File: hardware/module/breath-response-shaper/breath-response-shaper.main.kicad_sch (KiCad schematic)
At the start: 13 parts

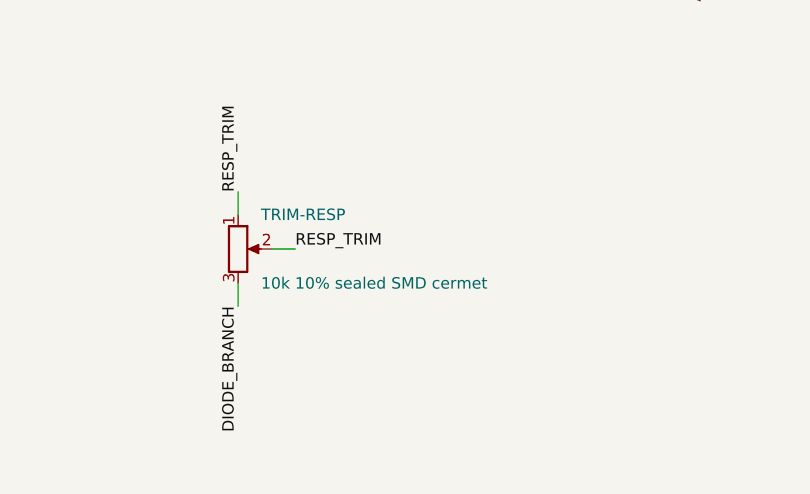
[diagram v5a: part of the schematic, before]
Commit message: #32: checkpoint - the owner's three answers and side-adjust trimmers
Owner decisions of 2026-10-04, recorded in ADR 0003/0004/0023/0024:
- WIDE's CMRR requirement band is DC to 7 kHz ("Keep 10 kHz, accept");
  cmrr-wide holds 58.5 dB there and records 10 kHz.
- D-TVS-BREATH is the PESD12VL1BA (19 pF), datasheet banked; PWR_GND
  held under -60 dB in each mode's band, WIDE at the accepted figure.
- The -12 V offset leg is filtered: R-BREATH-OFFNEG-A/-B 47.5k with
  C-BREATH-OFFNEG 1 uF at the split (6.7 Hz). Rest level +16 mV.
- The four trimmers are Bourns 3296X side-adjust, set with the module
  out of the rack; no rear-access windows. Current 3296 datasheet banked.

Sims are mid-run; their results land in the next commit.

Gate-Red: sim results stale or pre-change for receive-stage, power-entry, pitch-stage, mod-channels, shaper, system, breath-excitation-reference, digital-and-supervision and panel-led while they re-run on these inputs (checkpoint, as asked every 45 min); module-main and main-board .kicad_pcb parity with the new/changed parts (layout's, not touched here); main-board fab stale against the breath-adc sheet; module-main's existing routing/silk/acid-trap failures.

Co-Authored-By: Claude Opus 5.5 <noreply@anthropic.com>
Claude-Session: https://claude.ai/code/session_01LmB4muFXnoLprWX4JzuJ5A
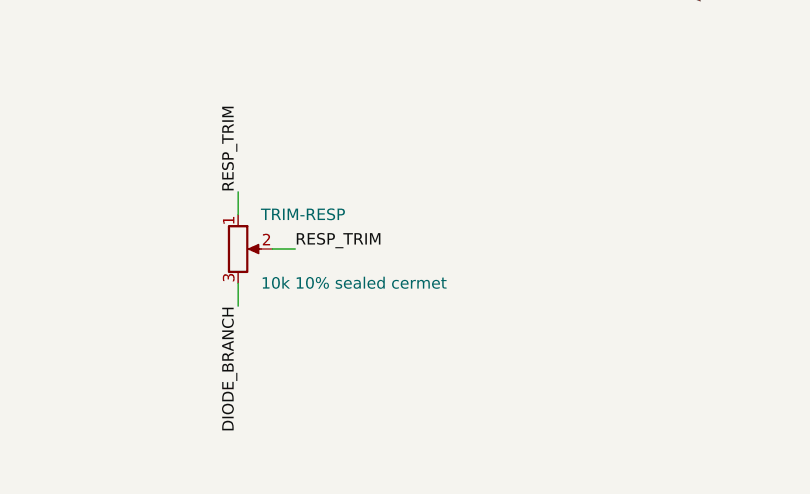
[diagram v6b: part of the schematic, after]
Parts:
- TRIM-RESP: value 10k 10% sealed SMD cermet -> 10k 10% sealed cermet; footprint Potentiometer_SMD:Potentiometer_Bourns_3224W_Vertical -> Potentiometer_THT:Potentiometer_Bourns_3296X_Horizontal; LCSC C81348 -> C111776; MPN 3224W-1-103E -> 3296X-1-103LF; Pins_source datasheets/discrete-and-power/BOURNS-3224-TRIMPOT.pdf p.1 s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 -> datasheets/discrete-and-power/BOURNS-3296-TRIMPOT.pdf p.1 c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
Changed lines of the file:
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@@
     (in_bom yes) (on_board yes) (dnp no)
     (property "Reference" "TRIM-RESP" (at 144.78 229.87 0) (effects (font (size 1.27 1.27)) (justify left)))
-    (property "Value" "10k 10% sealed SMD cermet" (at 144.78 237.49 0) (effects (font (size 1.27 1.27)) (justify left)))
-    (property "Footprint" "Potentiometer_SMD:Potentiometer_Bourns_3224W_Vertical" (at 142.24 233.68 0) (effects (font (size 1.27 1.27)) hide))
+    (property "Value" "10k 10% sealed cermet" (at 144.78 237.49 0) (effects (font (size 1.27 1.27)) (justify left)))
+    (property "Footprint" "Potentiometer_THT:Potentiometer_Bourns_3296X_Horizontal" (at 142.24 233.68 0) (effects (font (size 1.27 1.27)) hide))
     (property "Datasheet" "" (at 142.24 233.68 0) (effects (font (size 1.27 1.27)) hide))
     (property "Row" "TRIM-RESP" (at 142.24 233.68 0) (effects (font (size 1.27 1.27)) hide))
     (property "Pins" "CW=3(3) W=2(2) CCW=1(1)" (at 142.24 233.68 0) (effects (font (size 1.27 1.27)) hide))
     (property "Note" "IN SERIES with R-RESP, its wiper strapped to its CCW end, so clockwise LOWERS the branch's resistance and RAISES the exp end's gain - the panel knob's sense. An open wiper leaves the whole track in series: LESS gain, never more. Set once at commissioning (E10) to shaper-exp-gain's trimmed target at a hard blow, POT-RESP fully CW. module/breath-response-shaper/sim" (at 142.24 233.68 0) (effects (font (size 1.27 1.27)) hide))
-    (property "Pins_source" "datasheets/discrete-and-power/BOURNS-3224-TRIMPOT.pdf p.1 schematic: 1 CCW, 2 wiper, 3 CW" (at 142.24 233.68 0) (effects (font (size 1.27 1.27)) hide))
+    (property "Pins_source" "datasheets/discrete-and-power/BOURNS-3296-TRIMPOT.pdf p.1 circuit: 1 CCW, 2 wiper, 3 CW" (at 142.24 233.68 0) (effects (font (size 1.27 1.27)) hide))
     (property "Manufacturer" "Bourns" (at 142.24 233.68 0) (effects (font (size 1.27 1.27)) hide))
-    (property "MPN" "3224W-1-103E" (at 142.24 233.68 0) (effects (font (size 1.27 1.27)) hide))
-    (property "LCSC" "C81348" (at 142.24 233.68 0) (effects (font (size 1.27 1.27)) hide))
+    (property "MPN" "3296X-1-103LF" (at 142.24 233.68 0) (effects (font (size 1.27 1.27)) hide))
+    (property "LCSC" "C111776" (at 142.24 233.68 0) (effects (font (size 1.27 1.27)) hide))
     (property "Assembly" "hand" (at 142.24 233.68 0) (effects (font (size 1.27 1.27)) hide))
     (pin "1")
